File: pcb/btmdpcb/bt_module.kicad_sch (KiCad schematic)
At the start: 21 parts, among them J2 ANT, T1 ED8_4, T2 ED8_4

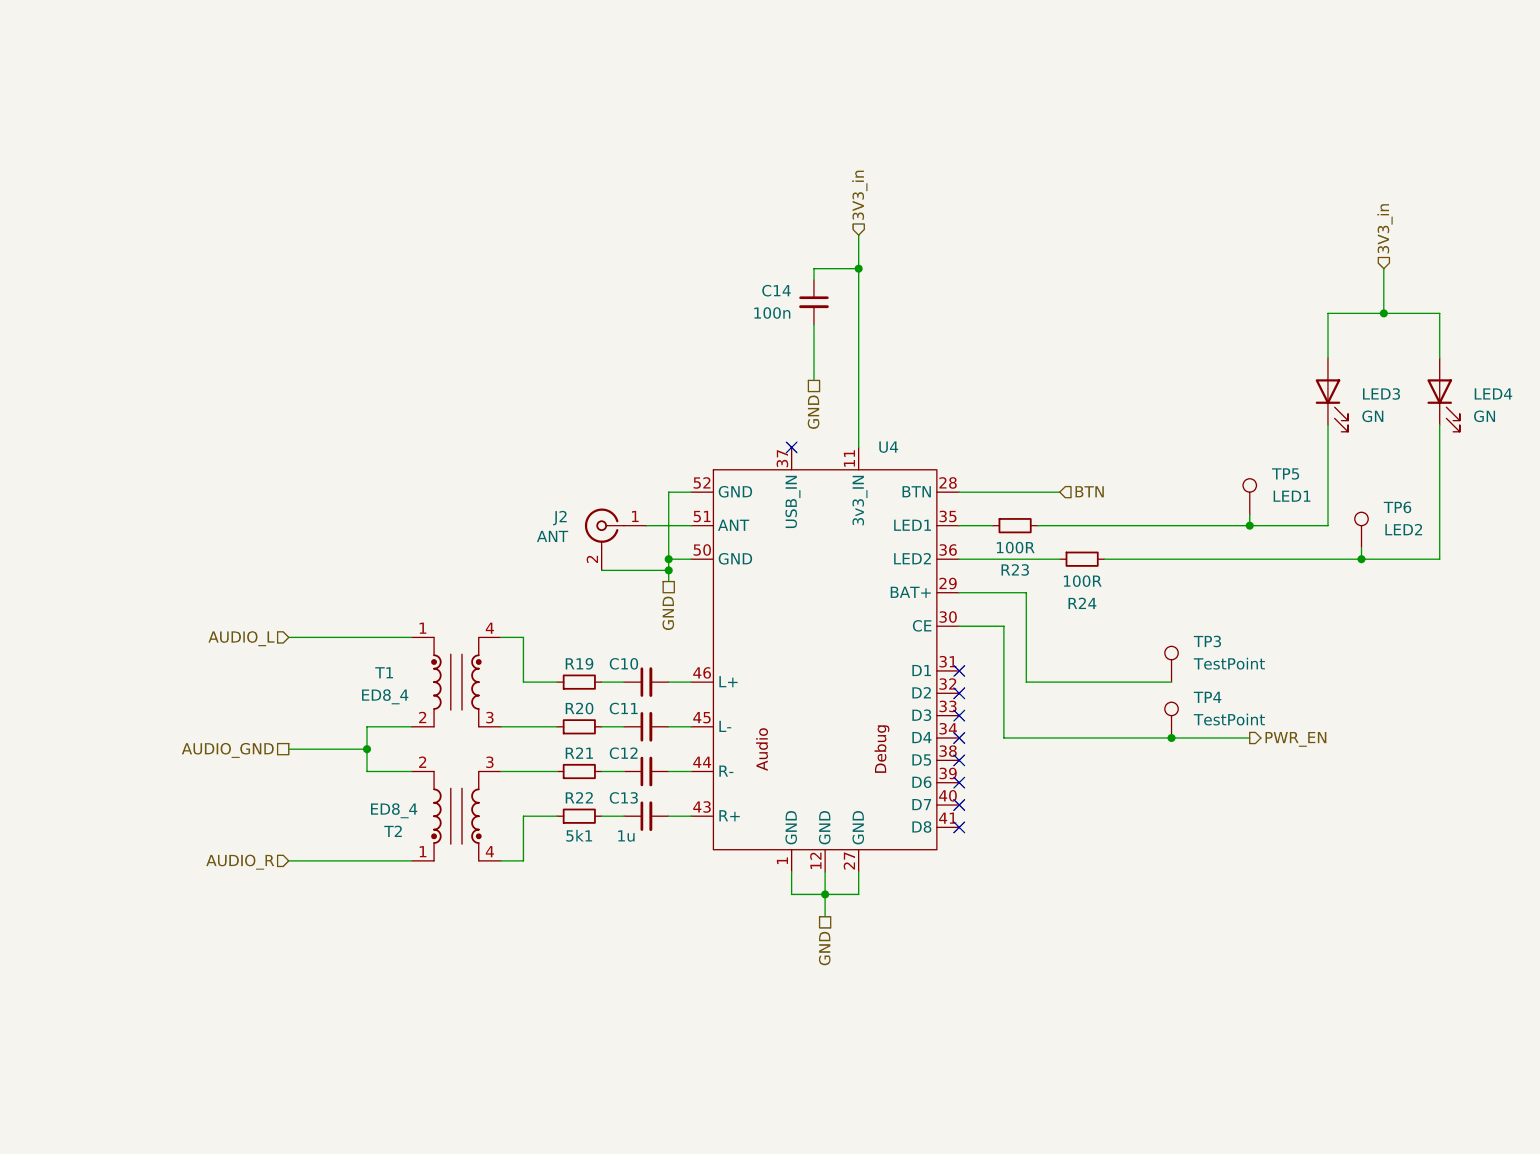
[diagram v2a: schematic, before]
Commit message: Add missing libraries, assign all footprints
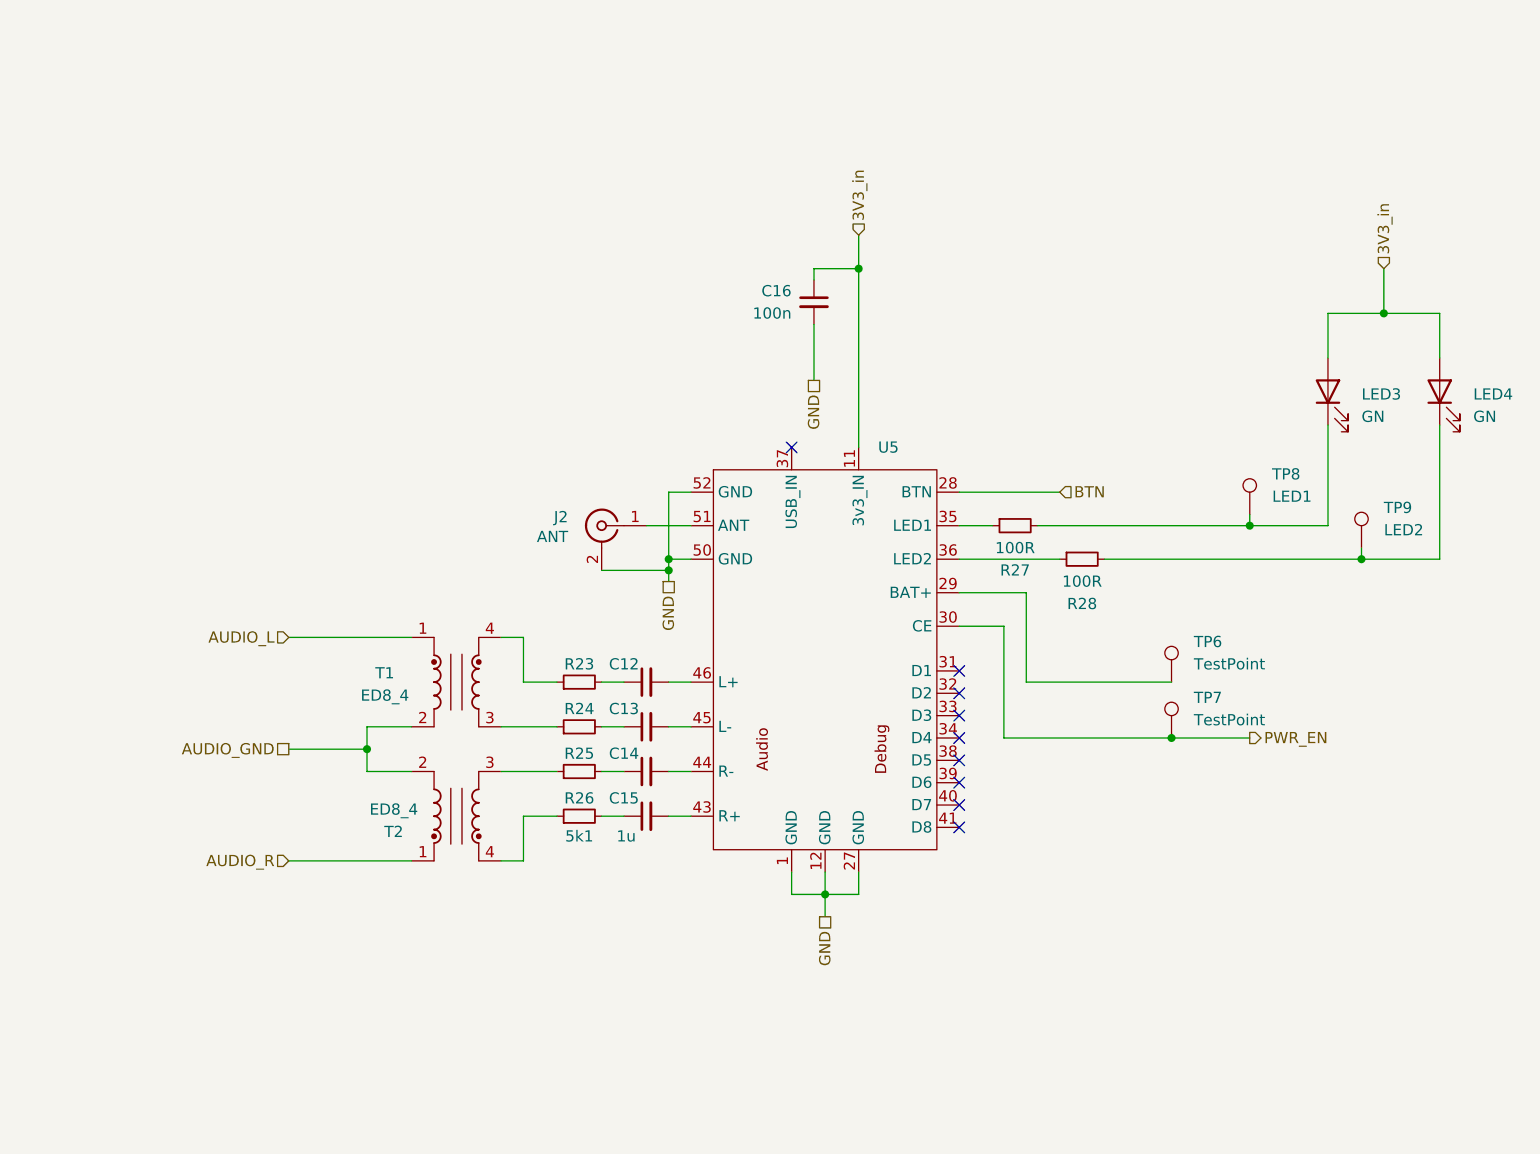
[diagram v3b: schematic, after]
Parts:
- C12: renamed from C10; footprint Capacitor_SMD:C_0603_1608Metric_Pad1.08x0.95mm_HandSolder -> Capacitor_SMD:C_0805_2012Metric_Pad1.18x1.45mm_HandSolder
- C13: renamed from C11; footprint Capacitor_SMD:C_0603_1608Metric_Pad1.08x0.95mm_HandSolder -> Capacitor_SMD:C_0805_2012Metric_Pad1.18x1.45mm_HandSolder
- C14: renamed from C12; footprint Capacitor_SMD:C_0603_1608Metric_Pad1.08x0.95mm_HandSolder -> Capacitor_SMD:C_0805_2012Metric_Pad1.18x1.45mm_HandSolder
- C15: renamed from C13; footprint Capacitor_SMD:C_0603_1608Metric_Pad1.08x0.95mm_HandSolder -> Capacitor_SMD:C_0805_2012Metric_Pad1.18x1.45mm_HandSolder
- C16: renamed from C14; footprint Capacitor_SMD:C_0603_1608Metric_Pad1.08x0.95mm_HandSolder -> Capacitor_SMD:C_0805_2012Metric_Pad1.18x1.45mm_HandSolder
- LED3, LED4: footprint LED_SMD:LED_0603_1608Metric_Pad1.05x0.95mm_HandSolder -> LED_SMD:LED_0805_2012Metric_Pad1.15x1.40mm_HandSolder
- R23: renamed from R19; footprint Resistor_SMD:R_0603_1608Metric_Pad0.98x0.95mm_HandSolder -> Resistor_SMD:R_0805_2012Metric_Pad1.20x1.40mm_HandSolder
- R24: renamed from R20; footprint Resistor_SMD:R_0603_1608Metric_Pad0.98x0.95mm_HandSolder -> Resistor_SMD:R_0805_2012Metric_Pad1.20x1.40mm_HandSolder
- R25: renamed from R21; footprint Resistor_SMD:R_0603_1608Metric_Pad0.98x0.95mm_HandSolder -> Resistor_SMD:R_0805_2012Metric_Pad1.20x1.40mm_HandSolder
- R26: renamed from R22; footprint Resistor_SMD:R_0603_1608Metric_Pad0.98x0.95mm_HandSolder -> Resistor_SMD:R_0805_2012Metric_Pad1.20x1.40mm_HandSolder
- R27: renamed from R23; footprint Resistor_SMD:R_0603_1608Metric_Pad0.98x0.95mm_HandSolder -> Resistor_SMD:R_0805_2012Metric_Pad1.20x1.40mm_HandSolder
- R28: renamed from R24; footprint Resistor_SMD:R_0603_1608Metric_Pad0.98x0.95mm_HandSolder -> Resistor_SMD:R_0805_2012Metric_Pad1.20x1.40mm_HandSolder
- renumbered TP3 to TP6, TP4 to TP7, TP5 to TP8, TP6 to TP9, U4 to U5
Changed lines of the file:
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@@
 		(on_board yes)
 		(dnp no)
-		(property "Reference" "R19"
+		(property "Reference" "R23"
 			(at 111.76 99.568 90)
 			(effects
@@
 			)
 		)
-		(property "Footprint" "Resistor_SMD:R_0603_1608Metric_Pad0.98x0.95mm_HandSolder"
+		(property "Footprint" "Resistor_SMD:R_0805_2012Metric_Pad1.20x1.40mm_HandSolder"
 			(at 111.76 101.6 0)
 			(effects
@@
 			(project "btmdpcb"
 				(path "/6e43e92f-e106-411c-86ee-217d084aee5b/5e29ed5f-7cd2-4605-9d5a-4da2465d4bbc"
-					(reference "R19")
+					(reference "R23")
 					(unit 1)
 				)
@@
 		(dnp no)
 		(fields_autoplaced yes)
-		(property "Reference" "TP3"
+		(property "Reference" "TP6"
 			(at 181.61 97.0279 0)
 			(effects
@@
 			(project "btmdpcb"
 				(path "/6e43e92f-e106-411c-86ee-217d084aee5b/5e29ed5f-7cd2-4605-9d5a-4da2465d4bbc"
-					(reference "TP3")
+					(reference "TP6")
 					(unit 1)
 				)
@@
 		(on_board yes)
 		(dnp no)
-		(property "Reference" "R23"
+		(property "Reference" "R27"
 			(at 161.29 88.9 90)
 			(effects
@@
 			)
 		)
-		(property "Footprint" "Resistor_SMD:R_0603_1608Metric_Pad0.98x0.95mm_HandSolder"
+		(property "Footprint" "Resistor_SMD:R_0805_2012Metric_Pad1.20x1.40mm_HandSolder"
 			(at 161.29 83.82 0)
 			(effects
@@
 			(project "btmdpcb"
 				(path "/6e43e92f-e106-411c-86ee-217d084aee5b/5e29ed5f-7cd2-4605-9d5a-4da2465d4bbc"
-					(reference "R23")
+					(reference "R27")
 					(unit 1)
 				)
@@
 		(on_board yes)
 		(dnp no)
-		(property "Reference" "C11"
+		(property "Reference" "C13"
 			(at 116.84 104.648 90)
 			(effects
@@
 			)
 		)
-		(property "Footprint" "Capacitor_SMD:C_0603_1608Metric_Pad1.08x0.95mm_HandSolder"
+		(property "Footprint" "Capacitor_SMD:C_0805_2012Metric_Pad1.18x1.45mm_HandSolder"
 			(at 119.38 106.68 0)
 			(effects
@@
 			(project "btmdpcb"
 				(path "/6e43e92f-e106-411c-86ee-217d084aee5b/5e29ed5f-7cd2-4605-9d5a-4da2465d4bbc"
-					(reference "C11")
+					(reference "C13")
 					(unit 1)
 				)
@@
 		(on_board yes)
 		(dnp no)
-		(property "Reference" "TP5"
+		(property "Reference" "TP8"
 			(at 190.5 77.9779 0)
 			(effects
@@
 			(project "btmdpcb"
 				(path "/6e43e92f-e106-411c-86ee-217d084aee5b/5e29ed5f-7cd2-4605-9d5a-4da2465d4bbc"
-					(reference "TP5")
+					(reference "TP8")
 					(unit 1)
 				)
@@
 		(on_board yes)
 		(dnp no)
-		(property "Reference" "R22"
+		(property "Reference" "R26"
 			(at 111.76 114.808 90)
 			(effects
@@
 			)
 		)
-		(property "Footprint" "Resistor_SMD:R_0603_1608Metric_Pad0.98x0.95mm_HandSolder"
+		(property "Footprint" "Resistor_SMD:R_0805_2012Metric_Pad1.20x1.40mm_HandSolder"
 			(at 111.76 116.84 0)
 			(effects
@@
 			(project "btmdpcb"
 				(path "/6e43e92f-e106-411c-86ee-217d084aee5b/5e29ed5f-7cd2-4605-9d5a-4da2465d4bbc"
-					(reference "R22")
+					(reference "R26")
 					(unit 1)
 				)
@@
 		(on_board yes)
 		(dnp no)
-		(property "Reference" "R24"
+		(property "Reference" "R28"
 			(at 168.91 92.71 90)
 			(effects
@@
 			)
 		)
-		(property "Footprint" "Resistor_SMD:R_0603_1608Metric_Pad0.98x0.95mm_HandSolder"
+		(property "Footprint" "Resistor_SMD:R_0805_2012Metric_Pad1.20x1.40mm_HandSolder"
 			(at 168.91 87.63 0)
 			(effects
@@
 			(project "btmdpcb"
 				(path "/6e43e92f-e106-411c-86ee-217d084aee5b/5e29ed5f-7cd2-4605-9d5a-4da2465d4bbc"
-					(reference "R24")
+					(reference "R28")
 					(unit 1)
 				)
@@
 		(on_board yes)
 		(dnp no)
-		(property "Reference" "R20"
+		(property "Reference" "R24"
 			(at 111.76 104.648 90)
 			(effects
@@
 			)
 		)
-		(property "Footprint" "Resistor_SMD:R_0603_1608Metric_Pad0.98x0.95mm_HandSolder"
+		(property "Footprint" "Resistor_SMD:R_0805_2012Metric_Pad1.20x1.40mm_HandSolder"
 			(at 111.76 106.68 0)
 			(effects
@@
 			(project "btmdpcb"
 				(path "/6e43e92f-e106-411c-86ee-217d084aee5b/5e29ed5f-7cd2-4605-9d5a-4da2465d4bbc"
-					(reference "R20")
+					(reference "R24")
 					(unit 1)
 				)
@@
 		(dnp no)
 		(fields_autoplaced yes)
-		(property "Reference" "TP4"
+		(property "Reference" "TP7"
 			(at 181.61 103.3779 0)
 			(effects
@@
 			(project "btmdpcb"
 				(path "/6e43e92f-e106-411c-86ee-217d084aee5b/5e29ed5f-7cd2-4605-9d5a-4da2465d4bbc"
-					(reference "TP4")
+					(reference "TP7")
 					(unit 1)
 				)
@@
 			)
 		)
-		(property "Footprint" "LED_SMD:LED_0603_1608Metric_Pad1.05x0.95mm_HandSolder"
+		(property "Footprint" "LED_SMD:LED_0805_2012Metric_Pad1.15x1.40mm_HandSolder"
 			(at 209.55 68.58 0)
 			(effects
@@
 		(on_board yes)
 		(dnp no)
-		(property "Reference" "R21"
+		(property "Reference" "R25"
 			(at 111.76 109.728 90)
 			(effects
@@
 			)
 		)
-		(property "Footprint" "Resistor_SMD:R_0603_1608Metric_Pad0.98x0.95mm_HandSolder"
+		(property "Footprint" "Resistor_SMD:R_0805_2012Metric_Pad1.20x1.40mm_HandSolder"
 			(at 111.76 111.76 0)
 			(effects
@@
 			(project "btmdpcb"
 				(path "/6e43e92f-e106-411c-86ee-217d084aee5b/5e29ed5f-7cd2-4605-9d5a-4da2465d4bbc"
-					(reference "R21")
+					(reference "R25")
 					(unit 1)
 				)
@@
 		(on_board yes)
 		(dnp no)
-		(property "Reference" "C12"
+		(property "Reference" "C14"
 			(at 116.84 109.728 90)
 			(effects
@@
 			)
 		)
-		(property "Footprint" "Capacitor_SMD:C_0603_1608Metric_Pad1.08x0.95mm_HandSolder"
+		(property "Footprint" "Capacitor_SMD:C_0805_2012Metric_Pad1.18x1.45mm_HandSolder"
 			(at 119.38 111.76 0)
 			(effects
@@
 			(project "btmdpcb"
 				(path "/6e43e92f-e106-411c-86ee-217d084aee5b/5e29ed5f-7cd2-4605-9d5a-4da2465d4bbc"
-					(reference "C12")
+					(reference "C14")
 					(unit 1)
 				)
@@
 		(on_board yes)
 		(dnp no)
-		(property "Reference" "C10"
+		(property "Reference" "C12"
 			(at 116.84 99.568 90)
 			(effects
@@
 			)
 		)
-		(property "Footprint" "Capacitor_SMD:C_0603_1608Metric_Pad1.08x0.95mm_HandSolder"
+		(property "Footprint" "Capacitor_SMD:C_0805_2012Metric_Pad1.18x1.45mm_HandSolder"
 			(at 119.38 101.6 0)
 			(effects
@@
 			(project "btmdpcb"
 				(path "/6e43e92f-e106-411c-86ee-217d084aee5b/5e29ed5f-7cd2-4605-9d5a-4da2465d4bbc"
-					(reference "C10")
+					(reference "C12")
 					(unit 1)
 				)
@@
 		(on_board yes)
 		(dnp no)
-		(property "Reference" "C14"
+		(property "Reference" "C16"
 			(at 135.89 57.1562 0)
 			(effects
@@
 			)
 		)
-		(property "Footprint" "Capacitor_SMD:C_0603_1608Metric_Pad1.08x0.95mm_HandSolder"
+		(property "Footprint" "Capacitor_SMD:C_0805_2012Metric_Pad1.18x1.45mm_HandSolder"
 			(at 138.43 58.42 0)
 			(effects
@@
 			(project "btmdpcb"
 				(path "/6e43e92f-e106-411c-86ee-217d084aee5b/5e29ed5f-7cd2-4605-9d5a-4da2465d4bbc"
-					(reference "C14")
+					(reference "C16")
 					(unit 1)
 				)
@@
 		(on_board yes)
 		(dnp no)
-		(property "Reference" "C13"
+		(property "Reference" "C15"
 			(at 116.84 114.808 90)
 			(effects
@@
 			)
 		)
-		(property "Footprint" "Capacitor_SMD:C_0603_1608Metric_Pad1.08x0.95mm_HandSolder"
+		(property "Footprint" "Capacitor_SMD:C_0805_2012Metric_Pad1.18x1.45mm_HandSolder"
 			(at 119.38 116.84 0)
 			(effects
@@
 			(project "btmdpcb"
 				(path "/6e43e92f-e106-411c-86ee-217d084aee5b/5e29ed5f-7cd2-4605-9d5a-4da2465d4bbc"
-					(reference "C13")
+					(reference "C15")
 					(unit 1)
 				)
@@
 		(on_board yes)
 		(dnp no)
-		(property "Reference" "U4"
+		(property "Reference" "U5"
 			(at 145.7041 74.93 0)
 			(effects
@@
 			(project "btmdpcb"
 				(path "/6e43e92f-e106-411c-86ee-217d084aee5b/5e29ed5f-7cd2-4605-9d5a-4da2465d4bbc"
-					(reference "U4")
+					(reference "U5")
 					(unit 1)
 				)
@@
 		(on_board yes)
 		(dnp no)
-		(property "Reference" "TP6"
+		(property "Reference" "TP9"
 			(at 203.2 81.7879 0)
 			(effects
@@
 			(project "btmdpcb"
 				(path "/6e43e92f-e106-411c-86ee-217d084aee5b/5e29ed5f-7cd2-4605-9d5a-4da2465d4bbc"
-					(reference "TP6")
+					(reference "TP9")
 					(unit 1)
 				)
@@
 			)
 		)
-		(property "Footprint" "LED_SMD:LED_0603_1608Metric_Pad1.05x0.95mm_HandSolder"
+		(property "Footprint" "LED_SMD:LED_0805_2012Metric_Pad1.15x1.40mm_HandSolder"
 			(at 196.85 68.58 0)
 			(effects
